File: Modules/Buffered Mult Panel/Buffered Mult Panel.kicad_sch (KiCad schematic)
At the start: 44 parts, among them J1 TS_Jack_6.35mm_Sw, J10 TS_Jack_6.35mm_Sw, J100 IDC_02x05, J11 TS_Jack_6.35mm_Sw, J12 TS_Jack_6.35mm_Sw, J13 TS_Jack_6.35mm_Sw, J14 TS_Jack_6.35mm_Sw, J15 TS_Jack_6.35mm_Sw, J16 TS_Jack_6.35mm_Sw, J2 TS_Jack_6.35mm_Sw, J3 TS_Jack_6.35mm_Sw, J4 TS_Jack_6.35mm_Sw, J5 TS_Jack_6.35mm_Sw, J6 TS_Jack_6.35mm_Sw, J7 TS_Jack_6.35mm_Sw, J8 TS_Jack_6.35mm_Sw, J9 TS_Jack_6.35mm_Sw, U1 TL074, U2 TL074, U3 TL074

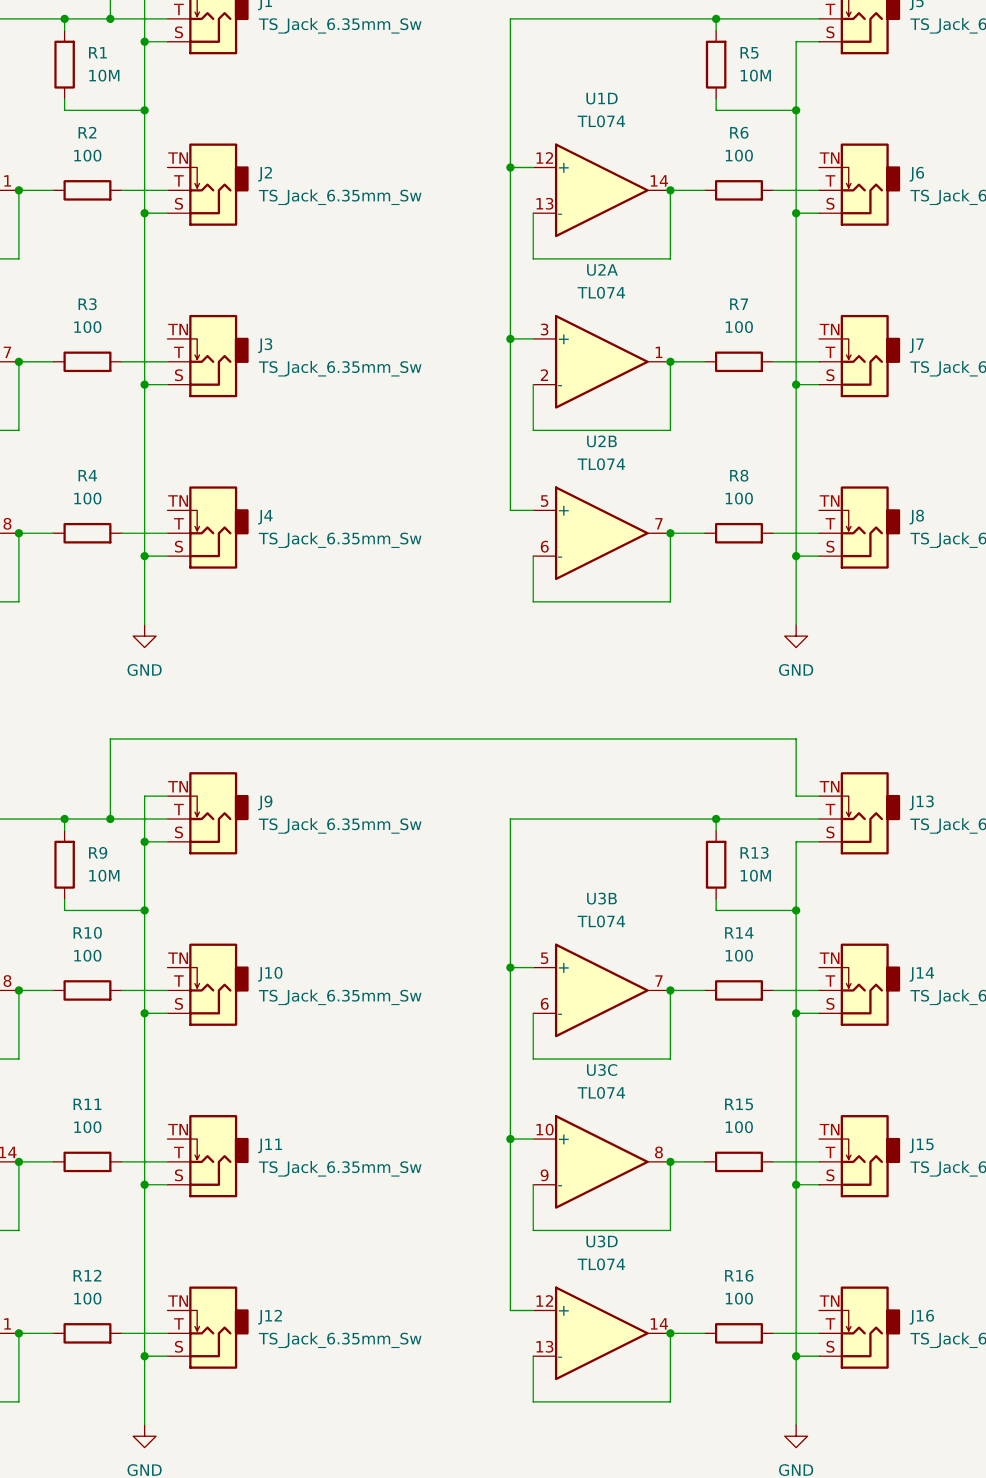
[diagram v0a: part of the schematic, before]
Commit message: Adjusted routing
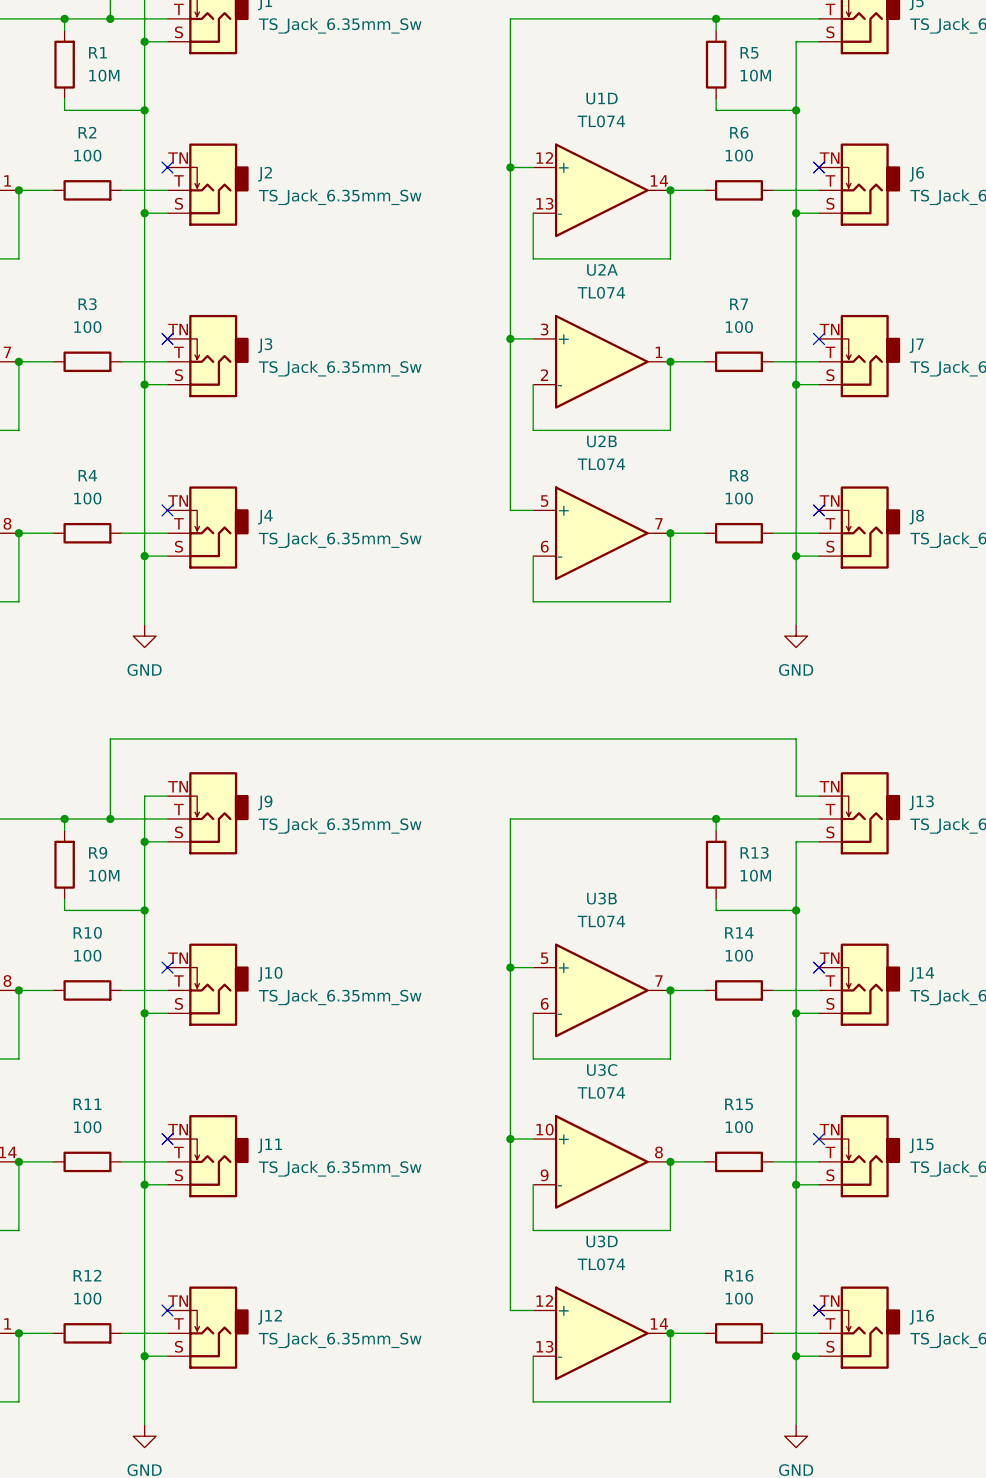
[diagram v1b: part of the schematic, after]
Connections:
- no-connect marks 0 -> 12
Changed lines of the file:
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@@
 		(color 0 0 0 0)
+	)
+	(no_connect
+		(at 53.34 128.27)
+	)
+	(no_connect
+		(at 125.73 77.47)
+	)
+	(no_connect
+		(at 125.73 147.32)
+	)
+	(no_connect
+		(at 53.34 77.47)
+	)
+	(no_connect
+		(at 53.34 39.37)
+	)
+	(no_connect
+		(at 125.73 166.37)
+	)
+	(no_connect
+		(at 125.73 128.27)
+	)
+	(no_connect
+		(at 125.73 58.42)
+	)
+	(no_connect
+		(at 53.34 166.37)
+	)
+	(no_connect
+		(at 53.34 147.32)
+	)
+	(no_connect
+		(at 53.34 58.42)
+	)
+	(no_connect
+		(at 125.73 39.37)
 	)
 	(wire

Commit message: Updated sch sheet title
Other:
- company: (none) -> DMH
- title: (none) -> Buffered Mult PCB
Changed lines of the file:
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@@
 	(generator_version "8.0")
 	(paper "A4")
+	(title_block
+		(title "Buffered Mult PCB")
+		(date "2024-05-31")
+		(rev "1")
+		(company "DMH")
+	)
 	(junction
 		(at 243.84 39.37)

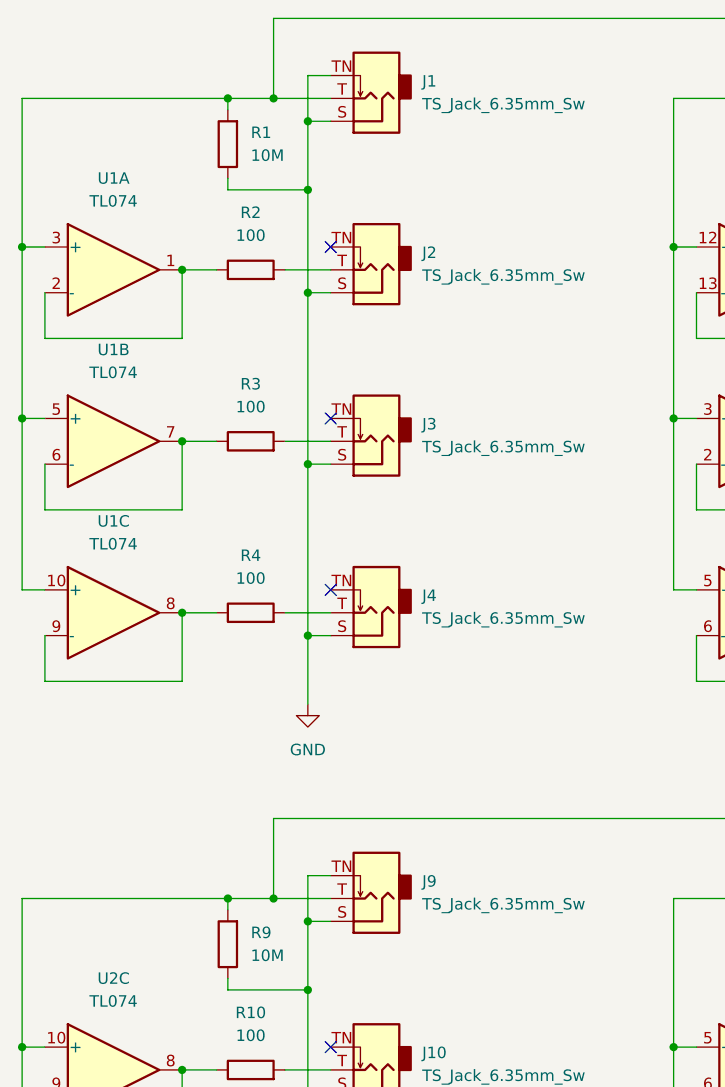
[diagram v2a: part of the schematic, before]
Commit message: Removed normalling of input jacks directly to GND
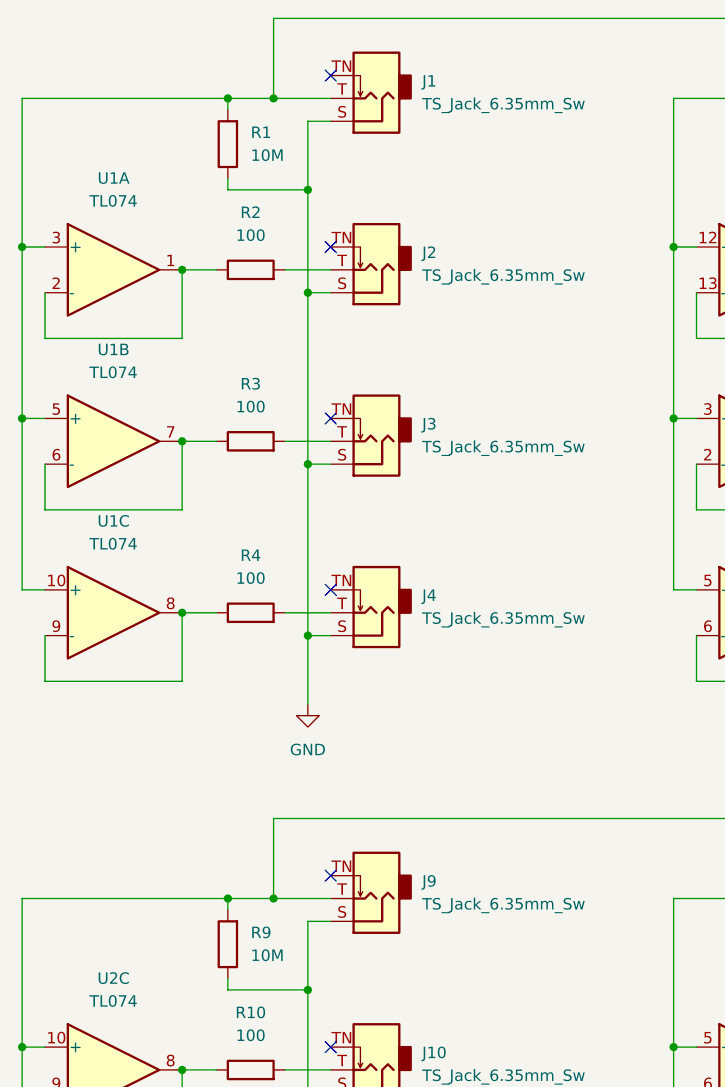
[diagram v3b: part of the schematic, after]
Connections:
- net GND: no longer J1.TN, J9.TN
- no-connect marks 12 -> 14
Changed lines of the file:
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@@
-	)
-	(junction
-		(at 50.8 114.3)
-		(diameter 0)
-		(color 0 0 0 0)
 	)
 	(junction
@@
 		(color 0 0 0 0)
 	)
-	(junction
-		(at 50.8 25.4)
-		(diameter 0)
-		(color 0 0 0 0)
+	(no_connect
+		(at 53.34 20.32)
 	)
 	(no_connect
@@
 	)
 	(no_connect
+		(at 53.34 109.22)
+	)
+	(no_connect
 		(at 125.73 147.32)
 	)
@@
 	(wire
 		(pts
-			(xy 53.34 109.22) (xy 50.8 109.22)
-		)
-		(stroke
-			(width 0)
-			(type default)
-		)
-	)
-	(wire
-		(pts
 			(xy 125.73 63.5) (xy 123.19 63.5)
 		)
@@
 	(wire
 		(pts
-			(xy 50.8 20.32) (xy 50.8 25.4)
-		)
-		(stroke
-			(width 0)
-			(type default)
-		)
-	)
-	(wire
-		(pts
 			(xy 50.8 63.5) (xy 53.34 63.5)
 		)
@@
 	(wire
 		(pts
-			(xy 50.8 109.22) (xy 50.8 114.3)
-		)
-		(stroke
-			(width 0)
-			(type default)
-		)
-	)
-	(wire
-		(pts
 			(xy 21.59 133.35) (xy 21.59 138.43)
 		)
@@
 		)
 		(stroke
-			(width 0)
-			(type default)
-		)
-	)
-	(wire
-		(pts
-			(xy 53.34 20.32) (xy 50.8 20.32)
-		)
-		(stroke

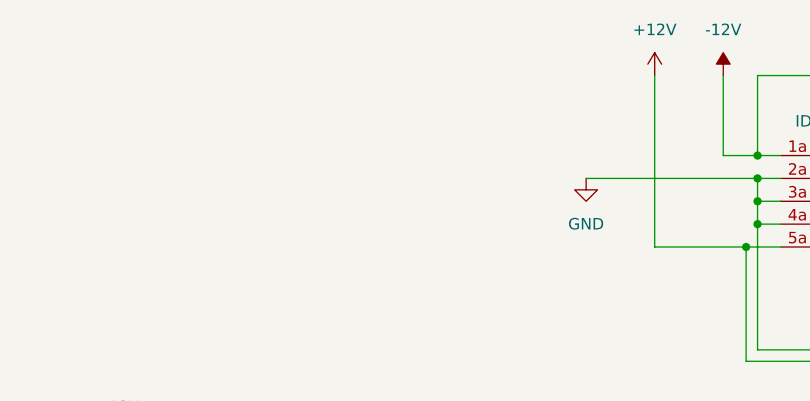
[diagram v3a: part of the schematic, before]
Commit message: Added 0V solder pad and pin to panel and PCB
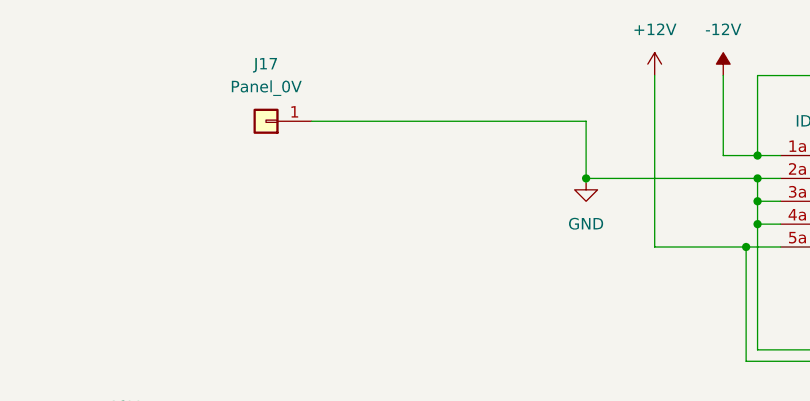
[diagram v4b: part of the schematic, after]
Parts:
- added J17: Panel_0V, Connector_PinHeader_2.54mm:PinHeader_1x01_P2.54mm_Vertical, symbol Connector_Generic:Conn_01x01
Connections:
- net GND: now also J17.1 (Pin_1)
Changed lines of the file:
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@@
 	)
 	(junction
+		(at 226.06 31.75)
+		(diameter 0)
+		(color 0 0 0 0)
+	)
+	(junction
 		(at 109.22 80.01)
 		(diameter 0)
@@
 	(wire
 		(pts
+			(xy 195.58 25.4) (xy 226.06 25.4)
+		)
+		(stroke
+			(width 0)
+			(type default)
+		)
+	)
+	(wire
+		(pts
 			(xy 50.8 33.02) (xy 50.8 44.45)
 		)
@@
 	(wire
 		(pts
+			(xy 226.06 25.4) (xy 226.06 31.75)
+		)
+		(stroke
+			(width 0)
+			(type default)
+		)
+	)
+	(wire
+		(pts
 			(xy 50.8 44.45) (xy 53.34 44.45)
 		)
@@
 				)
 			)
+		)
+	)
+	(symbol
+		(lib_id "Connector_Generic:Conn_01x01")
+		(at 190.5 25.4 180)
+		(unit 1)
+		(exclude_from_sim no)
+		(in_bom yes)
+		(on_board yes)
+		(dnp no)
+		(fields_autoplaced yes)
+		(property "Reference" "J17"
+			(at 190.5 19.05 0)
+			(effects
+				(font
+					(size 1.27 1.27)
+				)
+			)
+		)
+		(property "Value" "Panel_0V"
+			(at 190.5 21.59 0)
+			(effects
+				(font
+					(size 1.27 1.27)
+				)
+			)
+		)
+		(property "Footprint" "Connector_PinHeader_2.54mm:PinHeader_1x01_P2.54mm_Vertical"
+			(at 190.5 25.4 0)
+			(effects
+				(font
+					(size 1.27 1.27)
+				)
+				(hide yes)
+			)
+		)
+		(property "Datasheet" "~"
+			(at 190.5 25.4 0)
+			(effects
+				(font
+					(size 1.27 1.27)
+				)
+				(hide yes)
+			)
+		)
+		(property "Description" "Generic connector, single row, 01x01, script generated (kicad-library-utils/schlib/autogen/connector/)"
+			(at 190.5 25.4 0)
+			(effects
+				(font
+					(size 1.27 1.27)
+				)
+				(hide yes)
+			)
+		)
+		(pin "1"
+		)
+		(instances
+			(project ""
+				(path "/833651b9-9553-4eea-8a0e-30753753a6ae"
+					(reference "J17")
+					(unit 1)
+				)
+			)

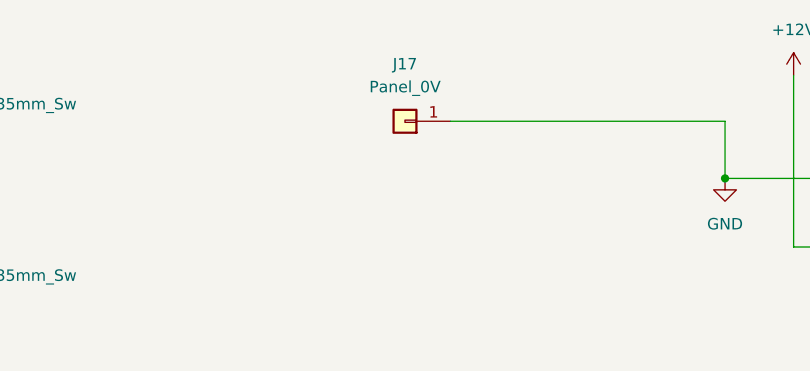
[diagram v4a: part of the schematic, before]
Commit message: Changed Panel 0V to Panel GND
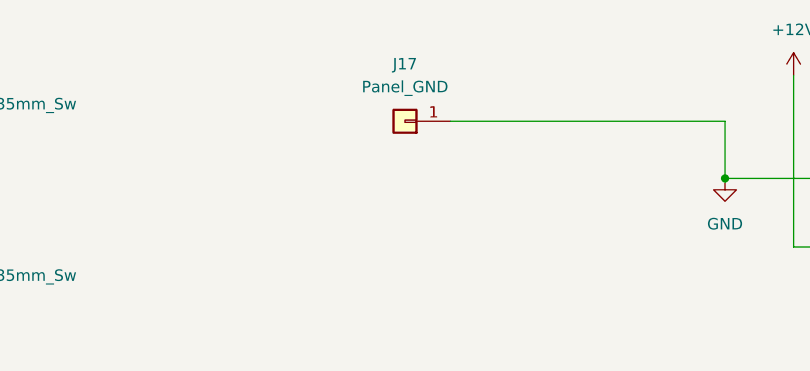
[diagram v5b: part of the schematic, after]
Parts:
- J17: value Panel_0V -> Panel_GND
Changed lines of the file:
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@@
 			)
 		)
-		(property "Value" "Panel_0V"
+		(property "Value" "Panel_GND"
 			(at 190.5 21.59 0)
 			(effects

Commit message: Replaced resistors with 1/4 W
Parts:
- R1, R10, R11, R12, R13, R14, R15, R16, R2, R3, R4, R5, R6, R7, R8, R9: footprint Resistor_THT:R_Axial_DIN0204_L3.6mm_D1.6mm_P5.08mm_Horizontal -> Resistor_THT:R_Axial_DIN0207_L6.3mm_D2.5mm_P7.62mm_Horizontal
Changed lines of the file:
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@@
 			)
 		)
-		(property "Footprint" "Resistor_THT:R_Axial_DIN0204_L3.6mm_D1.6mm_P5.08mm_Horizontal"
+		(property "Footprint" "Resistor_THT:R_Axial_DIN0207_L6.3mm_D2.5mm_P7.62mm_Horizontal"
 			(at 44.45 151.638 90)
 			(effects
@@
 			)
 		)
-		(property "Footprint" "Resistor_THT:R_Axial_DIN0204_L3.6mm_D1.6mm_P5.08mm_Horizontal"
+		(property "Footprint" "Resistor_THT:R_Axial_DIN0207_L6.3mm_D2.5mm_P7.62mm_Horizontal"
 			(at 43.688 27.94 90)
 			(effects
@@
 			)
 		)
-		(property "Footprint" "Resistor_THT:R_Axial_DIN0204_L3.6mm_D1.6mm_P5.08mm_Horizontal"
+		(property "Footprint" "Resistor_THT:R_Axial_DIN0207_L6.3mm_D2.5mm_P7.62mm_Horizontal"
 			(at 116.84 170.688 90)
 			(effects
@@
 			)
 		)
-		(property "Footprint" "Resistor_THT:R_Axial_DIN0204_L3.6mm_D1.6mm_P5.08mm_Horizontal"
+		(property "Footprint" "Resistor_THT:R_Axial_DIN0207_L6.3mm_D2.5mm_P7.62mm_Horizontal"
 			(at 44.45 62.738 90)
 			(effects
@@
 			)
 		)
-		(property "Footprint" "Resistor_THT:R_Axial_DIN0204_L3.6mm_D1.6mm_P5.08mm_Horizontal"
+		(property "Footprint" "Resistor_THT:R_Axial_DIN0207_L6.3mm_D2.5mm_P7.62mm_Horizontal"
 			(at 116.84 151.638 90)
 			(effects
@@
 			)
 		)
-		(property "Footprint" "Resistor_THT:R_Axial_DIN0204_L3.6mm_D1.6mm_P5.08mm_Horizontal"
+		(property "Footprint" "Resistor_THT:R_Axial_DIN0207_L6.3mm_D2.5mm_P7.62mm_Horizontal"
 			(at 44.45 132.588 90)
 			(effects
@@
 			)
 		)
-		(property "Footprint" "Resistor_THT:R_Axial_DIN0204_L3.6mm_D1.6mm_P5.08mm_Horizontal"
+		(property "Footprint" "Resistor_THT:R_Axial_DIN0207_L6.3mm_D2.5mm_P7.62mm_Horizontal"
 			(at 116.078 27.94 90)
 			(effects
@@
 			)
 		)
-		(property "Footprint" "Resistor_THT:R_Axial_DIN0204_L3.6mm_D1.6mm_P5.08mm_Horizontal"
+		(property "Footprint" "Resistor_THT:R_Axial_DIN0207_L6.3mm_D2.5mm_P7.62mm_Horizontal"
 			(at 116.84 43.688 90)
 			(effects
@@
 			)
 		)
-		(property "Footprint" "Resistor_THT:R_Axial_DIN0204_L3.6mm_D1.6mm_P5.08mm_Horizontal"
+		(property "Footprint" "Resistor_THT:R_Axial_DIN0207_L6.3mm_D2.5mm_P7.62mm_Horizontal"
 			(at 44.45 170.688 90)
 			(effects
@@
 			)
 		)
-		(property "Footprint" "Resistor_THT:R_Axial_DIN0204_L3.6mm_D1.6mm_P5.08mm_Horizontal"
+		(property "Footprint" "Resistor_THT:R_Axial_DIN0207_L6.3mm_D2.5mm_P7.62mm_Horizontal"
 			(at 44.45 81.788 90)
 			(effects
@@
 		)
 		(instances
-			(project ""
+			(project "Buffered Mult Panel"
 				(path "/833651b9-9553-4eea-8a0e-30753753a6ae"
 					(reference "J17")
@@
 			)
 		)
-		(property "Footprint" "Resistor_THT:R_Axial_DIN0204_L3.6mm_D1.6mm_P5.08mm_Horizontal"
+		(property "Footprint" "Resistor_THT:R_Axial_DIN0207_L6.3mm_D2.5mm_P7.62mm_Horizontal"
 			(at 116.84 62.738 90)
 			(effects
@@
 			)
 		)
-		(property "Footprint" "Resistor_THT:R_Axial_DIN0204_L3.6mm_D1.6mm_P5.08mm_Horizontal"
+		(property "Footprint" "Resistor_THT:R_Axial_DIN0207_L6.3mm_D2.5mm_P7.62mm_Horizontal"
 			(at 116.078 116.84 90)
 			(effects
@@
 			)
 		)
-		(property "Footprint" "Resistor_THT:R_Axial_DIN0204_L3.6mm_D1.6mm_P5.08mm_Horizontal"
+		(property "Footprint" "Resistor_THT:R_Axial_DIN0207_L6.3mm_D2.5mm_P7.62mm_Horizontal"
 			(at 44.45 43.688 90)
 			(effects
@@
 			)
 		)
-		(property "Footprint" "Resistor_THT:R_Axial_DIN0204_L3.6mm_D1.6mm_P5.08mm_Horizontal"
+		(property "Footprint" "Resistor_THT:R_Axial_DIN0207_L6.3mm_D2.5mm_P7.62mm_Horizontal"
 			(at 116.84 81.788 90)
 			(effects
@@
 			)
 		)
-		(property "Footprint" "Resistor_THT:R_Axial_DIN0204_L3.6mm_D1.6mm_P5.08mm_Horizontal"
+		(property "Footprint" "Resistor_THT:R_Axial_DIN0207_L6.3mm_D2.5mm_P7.62mm_Horizontal"
 			(at 43.688 116.84 90)
 			(effects
@@
 			)
 		)
-		(property "Footprint" "Resistor_THT:R_Axial_DIN0204_L3.6mm_D1.6mm_P5.08mm_Horizontal"
+		(property "Footprint" "Resistor_THT:R_Axial_DIN0207_L6.3mm_D2.5mm_P7.62mm_Horizontal"
 			(at 116.84 132.588 90)
 			(effects
